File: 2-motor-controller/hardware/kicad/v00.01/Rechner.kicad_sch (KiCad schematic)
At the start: 20 parts, among them Q601 BC337, Q602 BC337, Q603 BC337, Q604 BC337, SW601 B3F-4055, U601 ESP32-DevKitC-32E

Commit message: Motor-Controller: alle Blaetter nach den Zeichenregeln (Rahmen, Gruppen), 5-V-Zweig mit 2 x 4,7 uF, Titelfelder Version 00.01; Pruefung gegen Blockschaltbild 78/78
Co-Authored-By: Claude Opus 5.5 <noreply@anthropic.com>
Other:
- note added: "Belegung (geprüft mit Espressif ESP-IDF, GPIO): Startanschlüsse IO0, IO2, IO12 frei; IO5 und IO15 nur als Auswahlleitung (beim Start hoch). Pumpe (IO25–27) an Anschlüssen ohne Startfunktion. IO34–IO39 nur Eingang, ohne eigenen Widerstand: FLT (R11, Blatt Endstufe) und Taster (R609) ziehen nach +3,3 V. Taster abfragen, keinen Interrupt (Espressif: IO36/39 mit WLAN). IO16/17 frei nur ohne PSRAM (-3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"
- note removed: "Belegung: Startanschlüsse IO0, IO2, IO12 frei. IO34–IO39 nur Eingang, ohne eigenen Widerstand: FLT (R11 im Blatt Endstufe) und Taster (R609) ziehen nach +3,3 V. Flash (D0–D3, CMD, CLK) und USB-Seriell (TX, RX) frei. Wandler über VSPI (IO18, IO19, IO23, IO5). +3V3 kommt vom Regler auf dem Modul."
- company: (none) -> SuAn-Autopilot-Projekt
- title: (none) -> Motor-Controller V2.0 – Rechner und Bedienung
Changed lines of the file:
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@@
 	(generator_version "10.0")
 	(paper "A3")
+	(title_block
+		(title "Motor-Controller V2.0 – Rechner und Bedienung")
+		(date "2026-10-09")
+		(rev "00.01")
+		(company "SuAn-Autopilot-Projekt")
+	)
 	(rectangle
 		(start 12.7 17.78)
-		(end 149.86 142.24)
+		(end 149.86 147.32)
 		(stroke
 			(width 0)
@@
 		)
 	)
-	(text "Belegung: Startanschlüsse IO0, IO2, IO12 frei. IO34–IO39 nur Eingang, ohne eigenen\nWiderstand: FLT (R11 im Blatt Endstufe) und Taster (R609) ziehen nach +3,3 V.\nFlash (D0–D3, CMD, CLK) und USB-Seriell (TX, RX) frei. Wandler über VSPI\n(IO18, IO19, IO23, IO5). +3V3 kommt vom Regler auf dem Modul."
+	(text "Belegung (geprüft mit Espressif ESP-IDF, GPIO): Startanschlüsse IO0, IO2, IO12 frei;\nIO5 und IO15 nur als Auswahlleitung (beim Start hoch). Pumpe (IO25–27) an Anschlüssen\nohne Startfunktion. IO34–IO39 nur Eingang, ohne eigenen Widerstand: FLT (R11,\nBlatt Endstufe) und Taster (R609) ziehen nach +3,3 V. Taster abfragen, keinen Interrupt\n(Espressif: IO36/39 mit WLAN). IO16/17 frei nur ohne PSRAM (-32E, -32UE; nicht WROVER).\nFlash (D0–D3, CMD, CLK) und USB-Seriell (TX, RX) frei. Wandler über VSPI."
 		(exclude_from_sim no)
-		(at 13.97 139.7 0)
-		(effects
-			(font
+		(at 13.97 144.78 0)
+		(effects
+			(font

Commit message: Motor-Controller: Bauteile vollstaendig gewaehlt, Strombegrenzung in Software
- Leisten Wuerth WR-PHD (Buchse 8,5 mm, Stift), Stehbolzen M2 x 12, Taster E-Switch TL1105NF250Q (Winkel),
  Referenz LM4040AIZ-2.5 (+-0,1 %), Sicherungshalter Schurter 0031.8201, Leuchtdioden Dialight 551 (Winkel, rechte Kante)
- Strombegrenzung in der Software (Hall-Sensor), R10 an VREF nicht bestueckt
- Display-Beleuchtung aus +5 V ueber R610 220 Ohm; Vorwiderstand gruen 270 Ohm
- Selbsttest laeuft staendig ohne Ruderbewegung; WLAN ohne aeussere Antenne
- Pruefskript pruefung_blockschaltbild.py im Projekt: 80/80, ERC 0 Fehler
- Bauteilauswahl 00.22, Stueckliste 00.18, Anforderungen 00.11, Blockschaltbild 00.06, Messgeraet 00.03,
  Systembeschreibung, TODO, CHRONIK (Lehre Schaltplan), CLAUDE.md (Arbeitsweg KiCad)

Co-Authored-By: Claude Opus 5.5 <noreply@anthropic.com>
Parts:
- added R610: 220, symbol Device:R
- R603: value 180 -> 270
- SW601: value B3F-4055 -> TL1105NF250Q
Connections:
- net +3V3: no longer DS601.19 (BLA)
- net +5V: now also R610.1
- new net: DS601.19 (BLA), R610.2
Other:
- note added: "Leuchtdioden Dialight 551 (Winkelgehäuse, rechte Platinenkante) von +5 V über BC337: Blau braucht ca. 3,2 V, mehr als ein 3,3-V-Anschluss sicher liefert. Ströme ca. 9–10 mA (gerechnet aus dem Datenblatt). Taster E-Switch TL1105 (Winkel, Stößel ragt seitlich aus dem Gehäuse). Taster: Beleuchtung hell und WLAN wieder ein. 10k nach +3,3 V, 100 nF entprellt."
- note added: "Seriell (PSB an Masse): RS = Auswahl, R/W = Daten, E = Takt. RST fest an +3,3 V. Beleuchtung aus +5 V über R610 (220 Ω, Betreiber): immer an und gedimmt, bei Störung hell; Q601 schaltet sie mit PWM von IO4. Der Strom bleibt unter 15 mA (gerechnet). Kontrast am Modul (Trimmer). DB0–DB7, V0, VOUT im seriellen Betrieb frei."
- note removed: "Leuchtdioden von +5 V über BC337 geschaltet: Grün und Blau brauchen ca. 3 V, mehr als ein 3,3-V-Anschluss sicher liefert. Vorwiderstände für ca. 9–11 mA (gerechnet), an die gekauften Leuchtdioden anpassen. Leuchtdioden in der Gehäusewand, Taster auf der Platine. Taster: Beleuchtung hell und WLAN wieder ein. 10k nach +3,3 V, 100 nF entprellt."
- note removed: "Seriell (PSB an Masse): RS = Auswahl, R/W = Daten, E = Takt. RST fest an +3,3 V. Beleuchtung immer an und gedimmt, bei Störung hell: Q601 schaltet sie mit PWM von IO4. Kontrast am Modul (Trimmer). DB0–DB7, V0, VOUT im seriellen Betrieb frei."
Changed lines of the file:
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@@
 	(wire
 		(pts
+			(xy 269.24 36.83)
 			(xy 269.24 43.18)
-			(xy 269.24 40.64)
 		)
 		(stroke
@@
 	(wire
 		(pts
-			(xy 269.24 40.64)
-			(xy 259.08 40.64)
+			(xy 269.24 29.21)
+			(xy 269.24 26.67)
 		)
 		(stroke
@@
 		)
 	)
-	(junction
-		(at 259.08 40.64)
-		(diameter 0)
-		(color 0 0 0 0)
-	)
 	(wire
 		(pts
@@
 		)
 	)
-	(text "Seriell (PSB an Masse): RS = Auswahl, R/W = Daten, E = Takt. RST fest an +3,3 V.\nBeleuchtung immer an und gedimmt, bei Störung hell: Q601 schaltet sie mit PWM von IO4.\nKontrast am Modul (Trimmer). DB0–DB7, V0, VOUT im seriellen Betrieb frei."
+	(text "Seriell (PSB an Masse): RS = Auswahl, R/W = Daten, E = Takt. RST fest an +3,3 V.\nBeleuchtung aus +5 V über R610 (220 Ω, Betreiber): immer an und gedimmt, bei Störung hell;\nQ601 schaltet sie mit PWM von IO4. Der Strom bleibt unter 15 mA (gerechnet).\nKontrast am Modul (Trimmer). DB0–DB7, V0, VOUT im seriellen Betrieb frei."
 		(exclude_from_sim no)
 		(at 158.75 104.14 0)
@@
 		)
 	)
-	(text "Leuchtdioden von +5 V über BC337 geschaltet: Grün und Blau brauchen ca. 3 V, mehr als ein\n3,3-V-Anschluss sicher liefert. Vorwiderstände für ca. 9–11 mA (gerechnet), an die gekauften\nLeuchtdioden anpassen. Leuchtdioden in der Gehäusewand, Taster auf der Platine.\nTaster: Beleuchtung hell und WLAN wieder ein. 10k nach +3,3 V, 100 nF entprellt."
+	(text "Leuchtdioden Dialight 551 (Winkelgehäuse, rechte Platinenkante) von +5 V über BC337: Blau braucht\nca. 3,2 V, mehr als ein 3,3-V-Anschluss sicher liefert. Ströme ca. 9–10 mA (gerechnet aus dem\nDatenblatt). Taster E-Switch TL1105 (Winkel, Stößel ragt seitlich aus dem Gehäuse).\nTaster: Beleuchtung hell und WLAN wieder ein. 10k nach +3,3 V, 100 nF entprellt."
 		(exclude_from_sim no)
 		(at 158.75 193.04 0)
@@
 	)
 	(symbol
+		(lib_id "Device:R")
+		(at 269.24 33.02 0)
+		(unit 1)
+		(body_style 1)
+		(exclude_from_sim no)
+		(in_bom yes)
+		(on_board yes)
+		(in_pos_files yes)
+		(dnp no)
+		(property "Reference" "R610"
+			(at 271.78 31.75 0)
+			(show_name no)
+			(do_not_autoplace no)
+			(effects
+				(font
+					(size 1.27 1.27)
+				)
+				(justify left)
+			)
+		)
+		(property "Value" "220"
+			(at 271.78 34.29 0)
+			(show_name no)
+			(do_not_autoplace no)
+			(effects
+				(font
+					(size 1.27 1.27)
+				)
+				(justify left)
+			)
+		)
+		(property "Footprint" ""
+			(at 269.24 33.02 0)
+			(hide yes)
+			(show_name no)
+			(do_not_autoplace no)
+			(effects
+				(font
+					(size 1.27 1.27)
+				)
+			)
+		)
+		(property "Datasheet" ""
+			(at 269.24 33.02 0)
+			(hide yes)
+			(show_name no)
+			(do_not_autoplace no)
+			(effects
+				(font
+					(size 1.27 1.27)
+				)
+			)
+		)
+		(property "Description" "Resistor"
+			(at 269.24 33.02 0)
+			(hide yes)
+			(show_name no)
+			(do_not_autoplace no)
+			(effects
+				(font
+					(size 1.27 1.27)
+				)
+			)
+		)
+		(pin "1"
+		)
+		(pin "2"
+		)
+		(instances
+			(project "Motor-Controller"
+				(path "/255b263c-8a60-4b67-92ab-70f539cf8eaf/5d3c9440-3bfd-4492-a97b-bd0a45e9f692"
+					(reference "R610")
+					(unit 1)
+				)
+			)
+		)
+	)
+	(symbol
+		(lib_id "power:+5V")
+		(at 269.24 26.67 0)
+		(unit 1)
+		(body_style 1)
+		(exclude_from_sim no)
+		(in_bom yes)
+		(on_board yes)
+		(in_pos_files yes)
+		(dnp no)
+		(property "Reference" "#PWR610"
+			(at 269.24 26.67 0)
+			(hide yes)
+			(show_name no)
+			(do_not_autoplace no)
+			(effects
+				(font
+					(size 1.27 1.27)
+				)
+			)
+		)
+		(property "Value" "+5V"
+			(at 269.24 23.114 0)
+			(show_name no)
+			(do_not_autoplace no)
+			(effects
+				(font
+					(size 1.27 1.27)
+				)
+			)
+		)
+		(property "Footprint" ""
+			(at 269.24 26.67 0)
+			(hide yes)
+			(show_name no)
+			(do_not_autoplace no)
+			(effects
+				(font
+					(size 1.27 1.27)
+				)
+			)
+		)
+		(property "Datasheet" ""
+			(at 269.24 26.67 0)
+			(hide yes)
+			(show_name no)
+			(do_not_autoplace no)
+			(effects
+				(font
+					(size 1.27 1.27)
+				)
+			)
+		)
+		(property "Description" "Power symbol creates a global label with name \\\"+5V\\\""
+			(at 269.24 26.67 0)
+			(hide yes)
+			(show_name no)
+			(do_not_autoplace no)
+			(effects
+				(font
+					(size 1.27 1.27)
+				)
+			)
+		)
+		(pin "1"
+		)
+		(instances
+			(project "Motor-Controller"
+				(path "/255b263c-8a60-4b67-92ab-70f539cf8eaf/5d3c9440-3bfd-4492-a97b-bd0a45e9f692"
+					(reference "#PWR610")
+					(unit 1)
+				)
+			)
+		)
+	)
+	(symbol
 		(lib_id "power:GND")
 		(at 259.08 81.28 0)
@@
 		(in_pos_files yes)
 		(dnp no)
-		(property "Reference" "#PWR610"
+		(property "Reference" "#PWR611"
 			(at 259.08 81.28 0)
 			(hide yes)
@@
 			(project "Motor-Controller"
 				(path "/255b263c-8a60-4b67-92ab-70f539cf8eaf/5d3c9440-3bfd-4492-a97b-bd0a45e9f692"
-					(reference "#PWR610")
+					(reference "#PWR611")
 					(unit 1)
 				)
@@
 		(in_pos_files yes)
 		(dnp no)
-		(property "Reference" "#PWR611"
+		(property "Reference" "#PWR612"
 			(at 269.24 99.06 0)
 			(hide yes)
@@
 			(project "Motor-Controller"
 				(path "/255b263c-8a60-4b67-92ab-70f539cf8eaf/5d3c9440-3bfd-4492-a97b-bd0a45e9f692"
-					(reference "#PWR611")
+					(reference "#PWR612")
 					(unit 1)
 				)
@@
 			)
 		)
-		(property "Value" "180"
+		(property "Value" "270"
 			(at 205.74 143.51 0)
 			(show_name no)
@@
 		(in_pos_files yes)
 		(dnp no)
-		(property "Reference" "#PWR612"
+		(property "Reference" "#PWR613"
 			(at 203.2 135.89 0)
 			(hide yes)
@@
 			(project "Motor-Controller"
 				(path "/255b263c-8a60-4b67-92ab-70f539cf8eaf/5d3c9440-3bfd-4492-a97b-bd0a45e9f692"
-					(reference "#PWR612")
+					(reference "#PWR613")
 					(unit 1)
 				)
@@
 		(in_pos_files yes)
 		(dnp no)
-		(property "Reference" "#PWR613"
+		(property "Reference" "#PWR614"
 			(at 203.2 175.26 0)
 			(hide yes)
@@
 			(project "Motor-Controller"
 				(path "/255b263c-8a60-4b67-92ab-70f539cf8eaf/5d3c9440-3bfd-4492-a97b-bd0a45e9f692"
-					(reference "#PWR613")
+					(reference "#PWR614")
 					(unit 1)
 				)
@@
 		(in_pos_files yes)
 		(dnp no)
-		(property "Reference" "#PWR614"
+		(property "Reference" "#PWR615"
 			(at 254 135.89 0)
 			(hide yes)
@@
 			(project "Motor-Controller"
 				(path "/255b263c-8a60-4b67-92ab-70f539cf8eaf/5d3c9440-3bfd-4492-a97b-bd0a45e9f692"
-					(reference "#PWR614")
+					(reference "#PWR615")
 					(unit 1)
 				)
@@
 		(in_pos_files yes)
 		(dnp no)
-		(property "Reference" "#PWR615"
+		(property "Reference" "#PWR616"
 			(at 254 175.26 0)
 			(hide yes)
@@
 			(project "Motor-Controller"
 				(path "/255b263c-8a60-4b67-92ab-70f539cf8eaf/5d3c9440-3bfd-4492-a97b-bd0a45e9f692"
-					(reference "#PWR615")
+					(reference "#PWR616")
 					(unit 1)
 				)
@@
 		(in_pos_files yes)
 		(dnp no)
-		(property "Reference" "#PWR616"
+		(property "Reference" "#PWR617"
 			(at 304.8 135.89 0)
 			(hide yes)
@@
 			(project "Motor-Controller"
 				(path "/255b263c-8a60-4b67-92ab-70f539cf8eaf/5d3c9440-3bfd-4492-a97b-bd0a45e9f692"
-					(reference "#PWR616")
+					(reference "#PWR617")
 					(unit 1)
 				)
@@
 		(in_pos_files yes)
 		(dnp no)
-		(property "Reference" "#PWR617"
+		(property "Reference" "#PWR618"
 			(at 304.8 175.26 0)
 			(hide yes)
@@
 			(project "Motor-Controller"
 				(path "/255b263c-8a60-4b67-92ab-70f539cf8eaf/5d3c9440-3bfd-4492-a97b-bd0a45e9f692"
-					(reference "#PWR617")
+					(reference "#PWR618")
 					(unit 1)
 				)
@@
 		(in_pos_files yes)
 		(dnp no)
-		(property "Reference" "#PWR618"
+		(property "Reference" "#PWR619"
 			(at 365.76 135.89 0)
 			(hide yes)
@@
 			(project "Motor-Controller"
 				(path "/255b263c-8a60-4b67-92ab-70f539cf8eaf/5d3c9440-3bfd-4492-a97b-bd0a45e9f692"
-					(reference "#PWR618")
+					(reference "#PWR619")
 					(unit 1)
 				)
@@
 			)
 		)
-		(property "Value" "B3F-4055"
+		(property "Value" "TL1105NF250Q"
 			(at 369.57 163.83 90)
 			(show_name no)
@@
 		(in_pos_files yes)
 		(dnp no)
-		(property "Reference" "#PWR619"
+		(property "Reference" "#PWR620"
 			(at 365.76 170.18 0)
 			(hide yes)
@@
 			(project "Motor-Controller"
 				(path "/255b263c-8a60-4b67-92ab-70f539cf8eaf/5d3c9440-3bfd-4492-a97b-bd0a45e9f692"
-					(reference "#PWR619")
+					(reference "#PWR620")
 					(unit 1)
 				)
@@
 		(in_pos_files yes)
 		(dnp no)
-		(property "Reference" "#PWR620"
+		(property "Reference" "#PWR621"
 			(at 388.62 170.18 0)
 			(hide yes)
@@
 			(project "Motor-Controller"
 				(path "/255b263c-8a60-4b67-92ab-70f539cf8eaf/5d3c9440-3bfd-4492-a97b-bd0a45e9f692"
-					(reference "#PWR620")
+					(reference "#PWR621")
 					(unit 1)
 				)

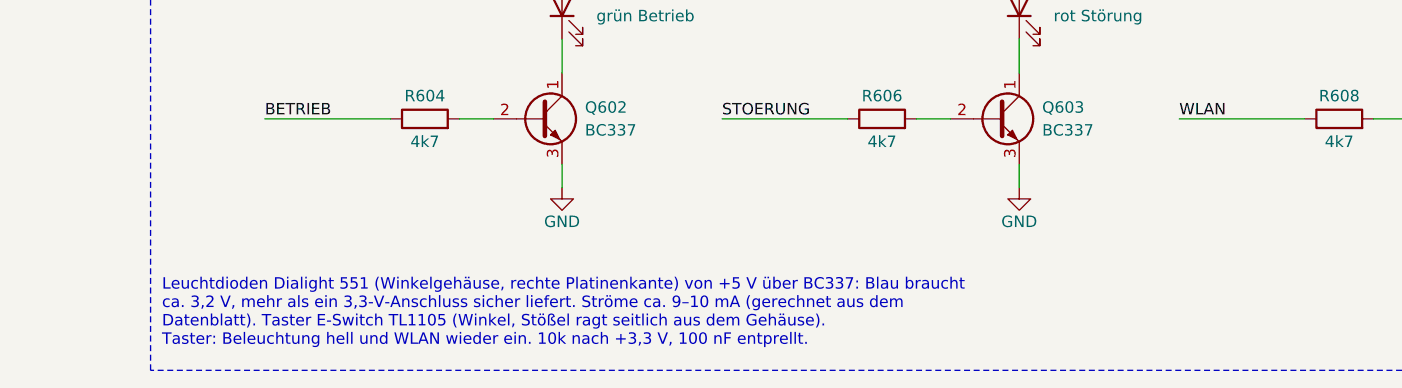
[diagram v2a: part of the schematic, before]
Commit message: Motor-Controller: Loetbilder zugeordnet (eigene: Dialight 551, TL1105, KEMET C320, Display-Leiste), Platine 150 x 130 mm mit allen 94 Teilen angeordnet - Bauteilauswahl 00.23, Anforderungen 00.11, Stueckliste 00.19
Co-Authored-By: Claude Opus 5.5 <noreply@anthropic.com>
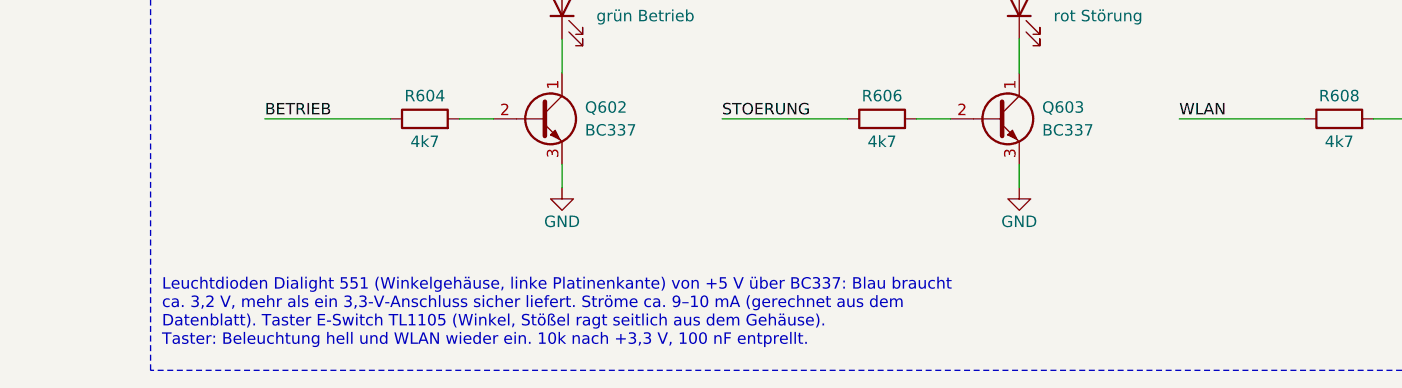
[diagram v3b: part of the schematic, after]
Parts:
- C601: footprint (none) -> Motor-Controller:C_KEMET_C320_L5.1mm_W4.1mm_P2.54mm
- D601, D602, D603: footprint (none) -> Motor-Controller:LED_Dialight_551_RightAngle
- DS601: footprint (none) -> Motor-Controller:LCD_12864B_Socket
- R601, R602, R603, R604, R605, R606, R607, R608, R609, R610: footprint (none) -> Resistor_THT:R_Axial_DIN0207_L6.3mm_D2.5mm_P10.16mm_Horizontal
- SW601: footprint (none) -> Motor-Controller:SW_E-Switch_TL1105_RightAngle
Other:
- note added: "Leuchtdioden Dialight 551 (Winkelgehäuse, linke Platinenkante) von +5 V über BC337: Blau braucht ca. 3,2 V, mehr als ein 3,3-V-Anschluss sicher liefert. Ströme ca. 9–10 mA (gerechnet aus dem Datenblatt). Taster E-Switch TL1105 (Winkel, Stößel ragt seitlich aus dem Gehäuse). Taster: Beleuchtung hell und WLAN wieder ein. 10k nach +3,3 V, 100 nF entprellt."
- note removed: "Leuchtdioden Dialight 551 (Winkelgehäuse, rechte Platinenkante) von +5 V über BC337: Blau braucht ca. 3,2 V, mehr als ein 3,3-V-Anschluss sicher liefert. Ströme ca. 9–10 mA (gerechnet aus dem Datenblatt). Taster E-Switch TL1105 (Winkel, Stößel ragt seitlich aus dem Gehäuse). Taster: Beleuchtung hell und WLAN wieder ein. 10k nach +3,3 V, 100 nF entprellt."
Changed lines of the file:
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@@
 		)
 	)
-	(text "Leuchtdioden Dialight 551 (Winkelgehäuse, rechte Platinenkante) von +5 V über BC337: Blau braucht\nca. 3,2 V, mehr als ein 3,3-V-Anschluss sicher liefert. Ströme ca. 9–10 mA (gerechnet aus dem\nDatenblatt). Taster E-Switch TL1105 (Winkel, Stößel ragt seitlich aus dem Gehäuse).\nTaster: Beleuchtung hell und WLAN wieder ein. 10k nach +3,3 V, 100 nF entprellt."
+	(text "Leuchtdioden Dialight 551 (Winkelgehäuse, linke Platinenkante) von +5 V über BC337: Blau braucht\nca. 3,2 V, mehr als ein 3,3-V-Anschluss sicher liefert. Ströme ca. 9–10 mA (gerechnet aus dem\nDatenblatt). Taster E-Switch TL1105 (Winkel, Stößel ragt seitlich aus dem Gehäuse).\nTaster: Beleuchtung hell und WLAN wieder ein. 10k nach +3,3 V, 100 nF entprellt."
 		(exclude_from_sim no)
 		(at 158.75 193.04 0)
@@
 			)
 		)
-		(property "Footprint" ""
+		(property "Footprint" "Resistor_THT:R_Axial_DIN0207_L6.3mm_D2.5mm_P10.16mm_Horizontal"
 			(at 55.88 114.3 0)
 			(hide yes)
@@
 			)
 		)
-		(property "Footprint" ""
+		(property "Footprint" "Motor-Controller:LCD_12864B_Socket"
 			(at 264.16 60.96 0)
 			(hide yes)
@@
 			)
 		)
-		(property "Footprint" ""
+		(property "Footprint" "Resistor_THT:R_Axial_DIN0207_L6.3mm_D2.5mm_P10.16mm_Horizontal"
 			(at 269.24 33.02 0)
 			(hide yes)
@@
 			)
 		)
-		(property "Footprint" ""
+		(property "Footprint" "Resistor_THT:R_Axial_DIN0207_L6.3mm_D2.5mm_P10.16mm_Horizontal"
 			(at 248.92 91.44 0)
 			(hide yes)
@@
 			)
 		)
-		(property "Footprint" ""
+		(property "Footprint" "Motor-Controller:LED_Dialight_551_RightAngle"
 			(at 203.2 154.94 0)
 			(hide yes)
@@
 			)
 		)
-		(property "Footprint" ""
+		(property "Footprint" "Resistor_THT:R_Axial_DIN0207_L6.3mm_D2.5mm_P10.16mm_Horizontal"
 			(at 203.2 142.24 0)
 			(hide yes)
@@
 			)
 		)
-		(property "Footprint" ""
+		(property "Footprint" "Resistor_THT:R_Axial_DIN0207_L6.3mm_D2.5mm_P10.16mm_Horizontal"
 			(at 187.96 167.64 0)
 			(hide yes)
@@
 			)
 		)
-		(property "Footprint" ""
+		(property "Footprint" "Motor-Controller:LED_Dialight_551_RightAngle"
 			(at 254 154.94 0)
 			(hide yes)
@@
 			)
 		)
-		(property "Footprint" ""
+		(property "Footprint" "Resistor_THT:R_Axial_DIN0207_L6.3mm_D2.5mm_P10.16mm_Horizontal"
 			(at 254 142.24 0)
 			(hide yes)
@@
 			)
 		)
-		(property "Footprint" ""
+		(property "Footprint" "Resistor_THT:R_Axial_DIN0207_L6.3mm_D2.5mm_P10.16mm_Horizontal"
 			(at 238.76 167.64 0)
 			(hide yes)
@@
 			)
 		)
-		(property "Footprint" ""
+		(property "Footprint" "Motor-Controller:LED_Dialight_551_RightAngle"
 			(at 304.8 154.94 0)
 			(hide yes)
@@
 			)
 		)
-		(property "Footprint" ""
+		(property "Footprint" "Resistor_THT:R_Axial_DIN0207_L6.3mm_D2.5mm_P10.16mm_Horizontal"
 			(at 304.8 142.24 0)
 			(hide yes)
@@
 			)
 		)
-		(property "Footprint" ""
+		(property "Footprint" "Resistor_THT:R_Axial_DIN0207_L6.3mm_D2.5mm_P10.16mm_Horizontal"
 			(at 289.56 167.64 0)
 			(hide yes)
@@
 			)
 		)
-		(property "Footprint" ""
+		(property "Footprint" "Resistor_THT:R_Axial_DIN0207_L6.3mm_D2.5mm_P10.16mm_Horizontal"
 			(at 365.76 142.24 0)
 			(hide yes)
@@
 			)
 		)
-		(property "Footprint" ""
+		(property "Footprint" "Motor-Controller:SW_E-Switch_TL1105_RightAngle"
 			(at 365.76 162.56 0)
 			(hide yes)
@@
 			)
 		)
-		(property "Footprint" ""
+		(property "Footprint" "Motor-Controller:C_KEMET_C320_L5.1mm_W4.1mm_P2.54mm"
 			(at 388.62 162.56 0)
 			(hide yes)
